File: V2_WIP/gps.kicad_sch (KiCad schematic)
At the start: 23 parts, among them U102 *W25Q128JFV, U103 ICM-45686

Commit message: updated list of changes in README.md
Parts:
- added C105, C106, C107: 100nF, Capacitor_SMD:C_0603_1608Metric_Pad1.08x0.95mm_HandSolder, symbol Device:C
- added IC1: OPT3001DNPR, KiCad:SON65P200X200X65-7N-D, symbol OPT3001DNPR:OPT3001DNPR
- added R109, R110: 0R, Resistor_SMD:R_0603_1608Metric_Pad0.98x0.95mm_HandSolder, symbol Device:R
- added R112, R113: 10, Resistor_SMD:R_0603_1608Metric_Pad0.98x0.95mm_HandSolder, symbol Device:R
- added R7, R8: 10k, Resistor_SMD:R_0603_1608Metric_Pad0.98x0.95mm_HandSolder, symbol Device:R
- added TP13: BMP_INT, TestPoint:TestPoint_Pad_D1.0mm, symbol Connector:TestPoint
- added TP14: OPT_INT, TestPoint:TestPoint_Pad_D1.0mm, symbol Connector:TestPoint
- added U2: BMP581, BMP581, symbol BMP581:BMP581
- D101: value +3V3 -> (none)
- D102: value +5V -> (none)
- D103: value VUSB -> (none)
- TP1, TP102, TP103, TP12, TP2, TP3, TP7: footprint TestPoint:TestPoint_Pad_D1.5mm -> TestPoint:TestPoint_Pad_D1.0mm
- U102: value *W25Q128JFV -> W25N02KVZEIR
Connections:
- net +3V3: now also C107.2, IC1.1 (VDD), R109.1, R112.1, R113.1, R7.1, R8.1
- net GND: now also C105.1, C106.1, C107.1, IC1.2 (ADDR), IC1.3 (GND), IC1.7 (EP), R110.2, U2.3 (VSS), U2.8 (VSS), U2.9 (VSS)
- net SCL_3V3: now also IC1.4 (SCL), R8.2, U2.2 (SCK)
- net SDA_3V3: now also IC1.6 (SDA), R7.2, U2.4 (SDI)
- new net: R109.2, R110.1, U2.5 (SDO)
- new net: IC1.5 (INT), TP14.1
- new net: C105.2, R112.2, U2.10 (VDD)
- new net: TP13.1, U2.7 (INT)
- new net VDDIO: C106.2, R113.2, U2.1 (VDDIO), U2.6 (CSB)
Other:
- note added: "Address selection"
- note added: "Změnit na WSON-8 8x6mm"
- moved on the sheet: C101, C103, C104, D101, D102, D103, R101, R102, R103, R104, R106, R_E101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

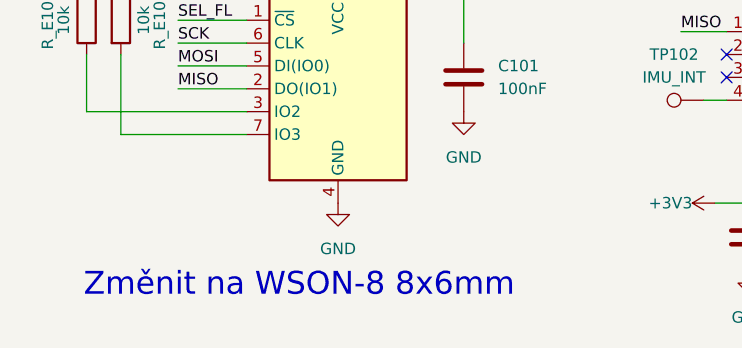
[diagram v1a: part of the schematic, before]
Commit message: changed footprints of U102 and U602
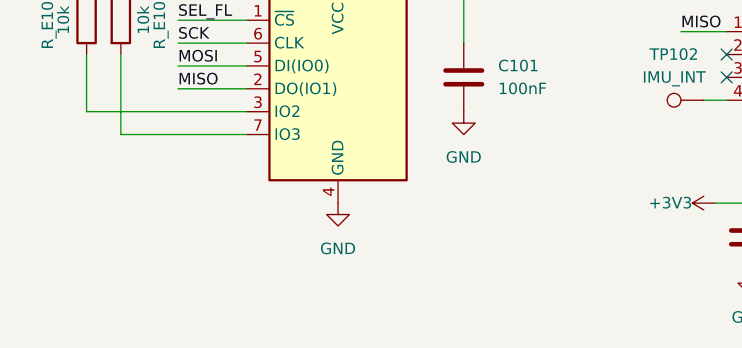
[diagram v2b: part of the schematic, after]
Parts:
- U102: footprint Package_SO:SOIC-8_5.23x5.23mm_P1.27mm -> Package_SON:WSON-8-1EP_8x6mm_P1.27mm_EP3.4x4.3mm
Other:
- note removed: "Změnit na WSON-8 8x6mm"
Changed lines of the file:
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@@
 		)
 	)
-	(text "Změnit na WSON-8 8x6mm\n"
-		(exclude_from_sim no)
-		(at 45.212 188.214 0)
-		(effects
-			(font
-				(size 2.54 2.54)
-				(color 255 0 9 1)
-			)
-		)
-	)
 	(text "FLASH"
 		(exclude_from_sim no)
@@
 			)
 		)
-		(property "Footprint" "Package_SO:SOIC-8_5.23x5.23mm_P1.27mm"
+		(property "Footprint" "Package_SON:WSON-8-1EP_8x6mm_P1.27mm_EP3.4x4.3mm"
 			(at 49.53 166.37 0)
 			(hide yes)

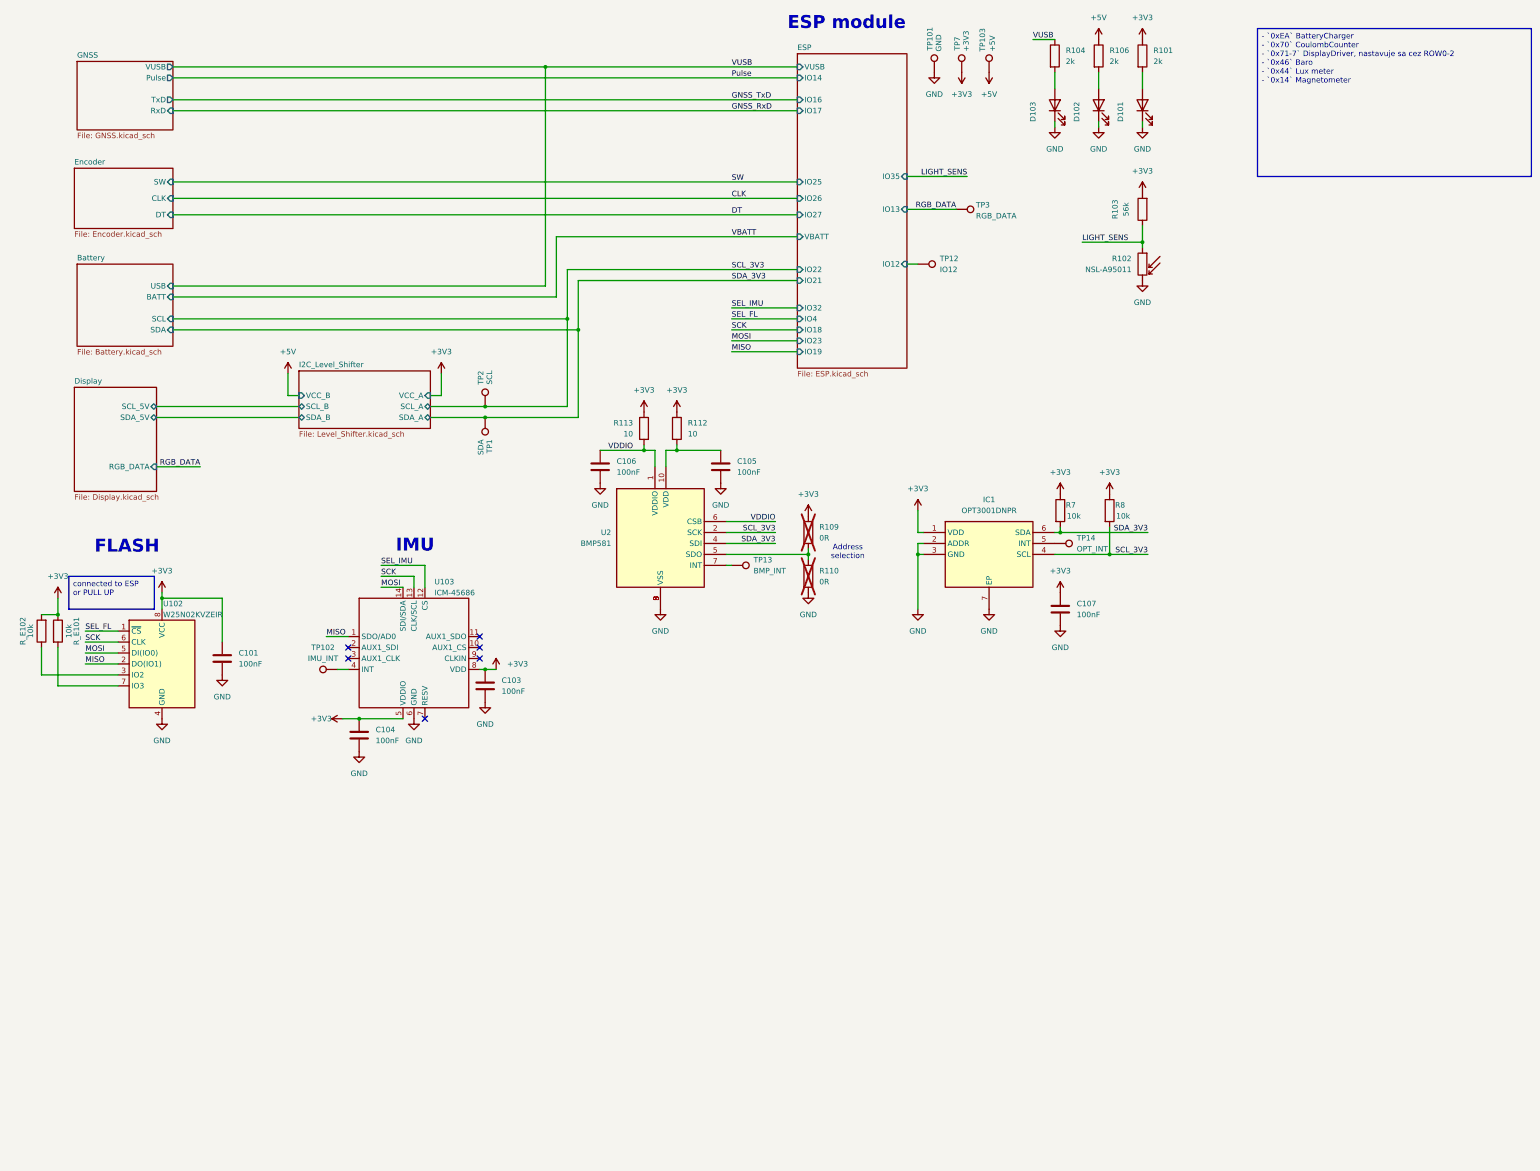
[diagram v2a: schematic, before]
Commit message: reworked the schematic, changed differential pairs and RF traces, small PCB adjustments
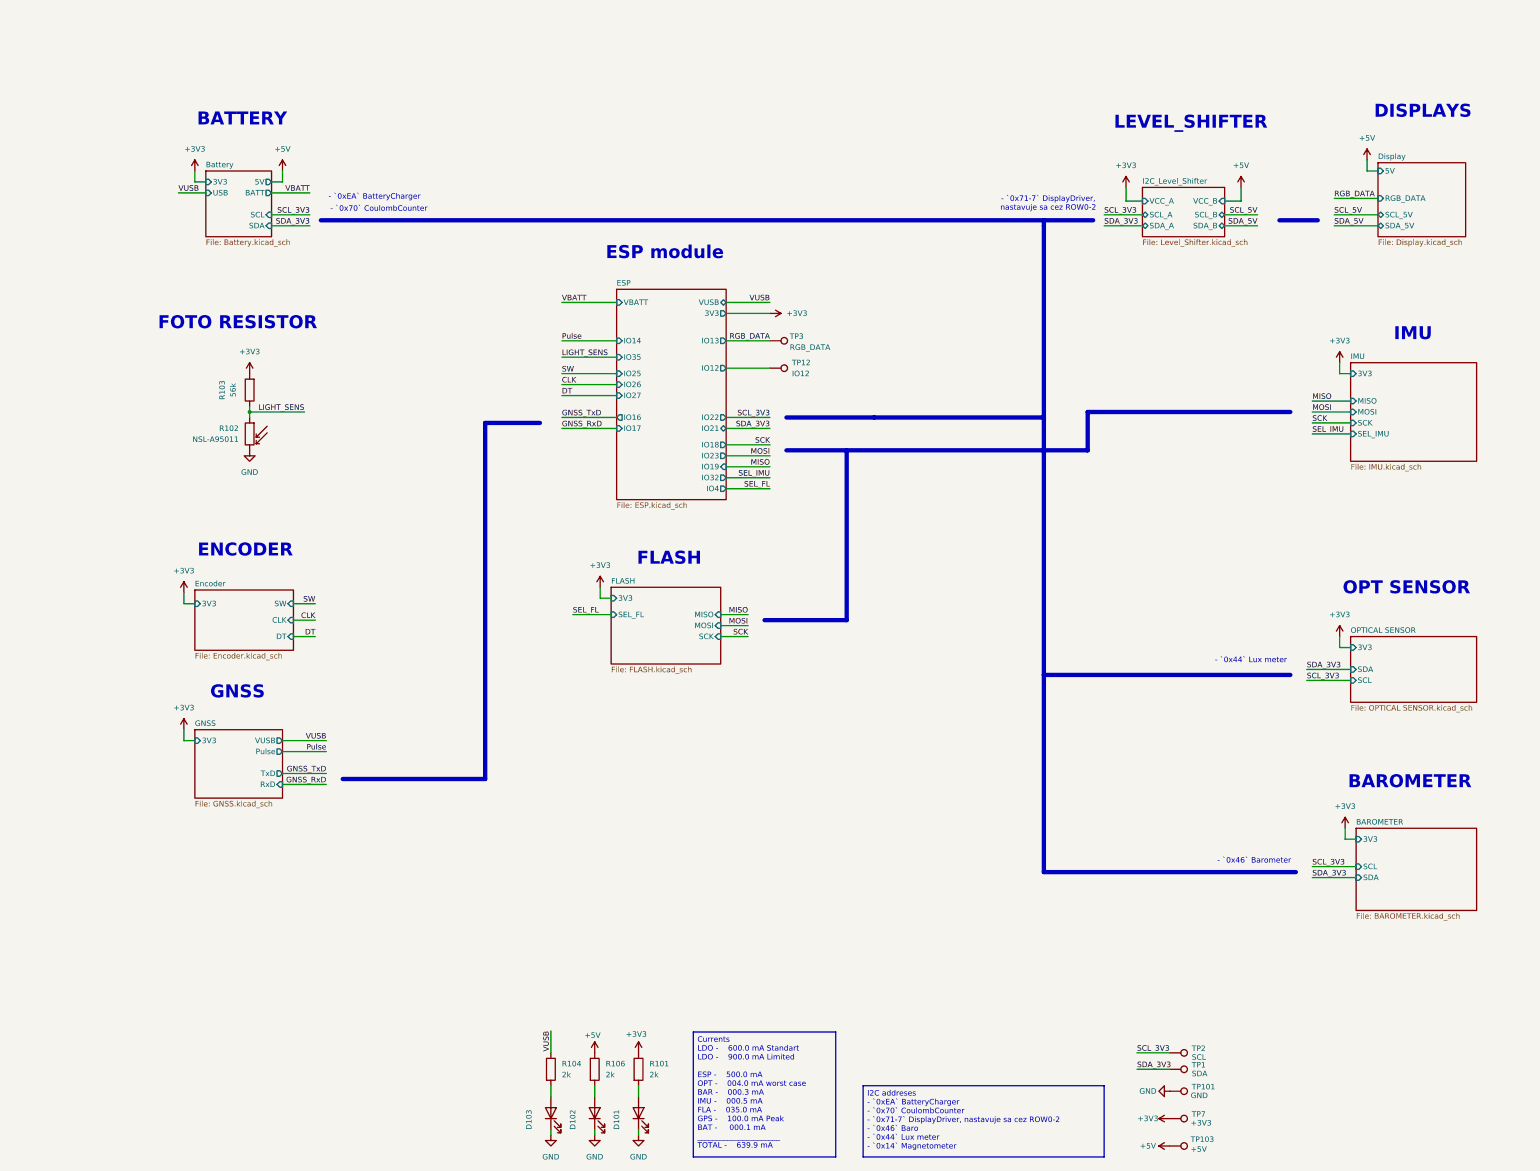
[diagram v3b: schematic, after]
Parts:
- removed C101, C103, C104, C105, C106, C107: 100nF, Capacitor_SMD:C_0603_1608Metric_Pad1.08x0.95mm_HandSolder, symbol Device:C
- removed IC1: OPT3001DNPR, KiCad:SON65P200X200X65-7N-D, symbol OPT3001DNPR:OPT3001DNPR
- removed R109, R110: 0R, Resistor_SMD:R_0603_1608Metric_Pad0.98x0.95mm_HandSolder, symbol Device:R
- removed R112, R113: 10, Resistor_SMD:R_0603_1608Metric_Pad0.98x0.95mm_HandSolder, symbol Device:R
- removed R7, R8, R_E101, R_E102: 10k, Resistor_SMD:R_0603_1608Metric_Pad0.98x0.95mm_HandSolder, symbol Device:R
- removed TP102: IMU_INT, TestPoint:TestPoint_Pad_D1.0mm, symbol Connector:TestPoint
- removed TP13: BMP_INT, TestPoint:TestPoint_Pad_D1.0mm, symbol Connector:TestPoint
- removed TP14: OPT_INT, TestPoint:TestPoint_Pad_D1.0mm, symbol Connector:TestPoint
- removed U102: W25N02KVZEIR, Package_SON:WSON-8-1EP_8x6mm_P1.27mm_EP3.4x4.3mm, symbol Memory_Flash:W25Q128JVS
- removed U103: ICM-45686, Package_LGA:LGA-14_3x2.5mm_P0.5mm_LayoutBorder3x4y, symbol icm-45686:ICM-45686
- removed U2: BMP581, BMP581, symbol BMP581:BMP581
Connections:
- no-connect marks 6 -> 0
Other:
- added sheet BAROMETER (BAROMETER.kicad_sch)
- added sheet FLASH (FLASH.kicad_sch)
- added sheet IMU (IMU.kicad_sch)
- added sheet OPTICAL SENSOR (OPTICAL SENSOR.kicad_sch)
- sheet Battery ports: added 3V3, 5V; removed none
- sheet Display ports: added 5V; removed none
- sheet ESP ports: added 3V3; removed none
- sheet Encoder ports: added 3V3; removed none
- sheet GNSS ports: added 3V3; removed none
- note added: "- `0x44` Lux meter"
- note added: "- `0x46` Barometer"
- note added: "- `0x70` CoulombCounter"
- note added: "- `0x71-7` DisplayDriver, nastavuje sa cez ROW0-2"
- note added: "- `0xEA` BatteryCharger"
- note added: "BAROMETER"
- note added: "BATTERY"
- note added: "DISPLAYS"
- note added: "ENCODER"
- note added: "FOTO RESISTOR"
- note added: "GNSS"
- note added: "LEVEL_SHIFTER"
- note added: "OPT SENSOR"
- note removed: "Address selection"
- moved on the sheet: D101, D102, D103, R101, R102, R103, R104, R106, TP101, TP103, TP12, TP3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
